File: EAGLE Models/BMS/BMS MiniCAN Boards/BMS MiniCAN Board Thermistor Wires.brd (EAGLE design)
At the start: 132.1 x 59.4 mm, 44 parts, among them IC1 AT90CAN128, IC2 MCP2551SO8, IC3 NUP2105L, IC5 FT232RL, Q1 56P2859, X10 8_PIN_CONN, X3 8_PIN_CONN, X4 8_PIN_CONN, X5 8_PIN_CONN, X6 8_PIN_CONN, X7 8_PIN_CONN, X8 8_PIN_CONN, X9 8_PIN_CONN

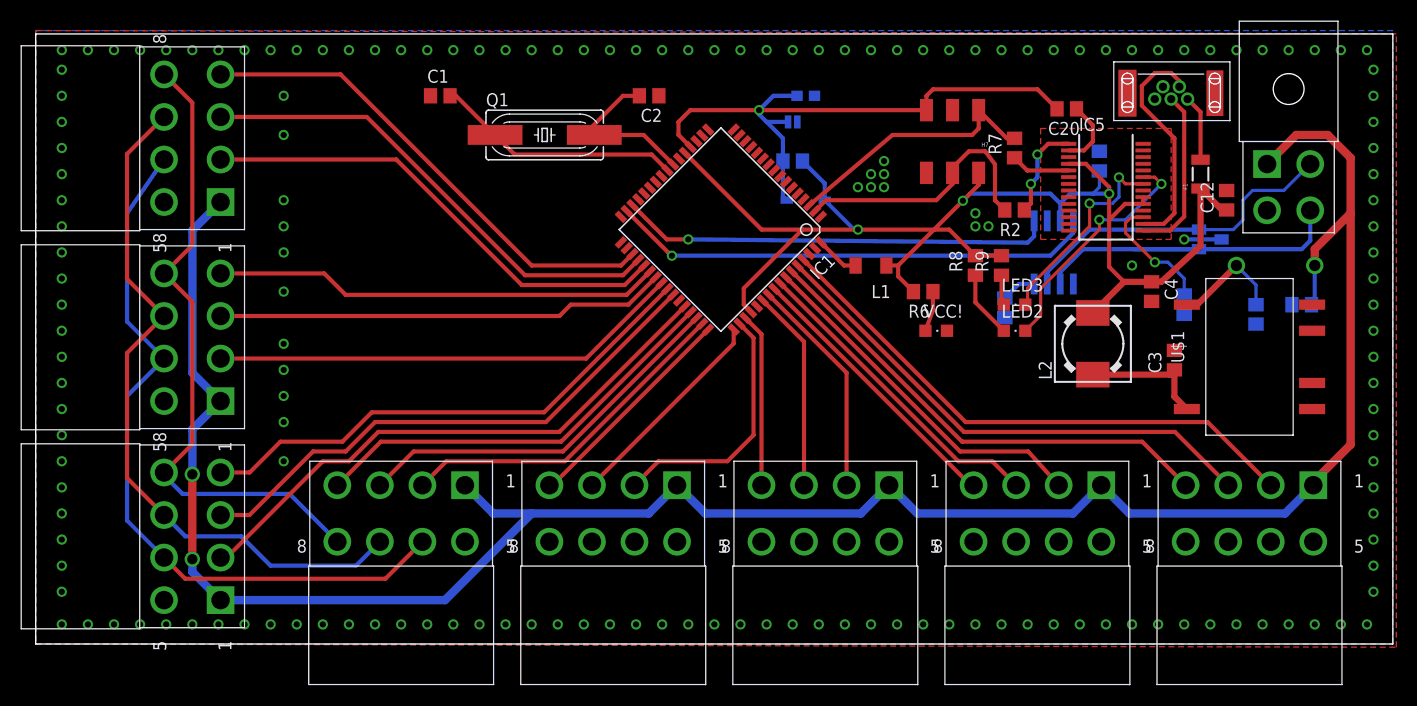
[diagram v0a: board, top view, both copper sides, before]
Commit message: Made minor changes. Added new board for different thermistor mounting strategy
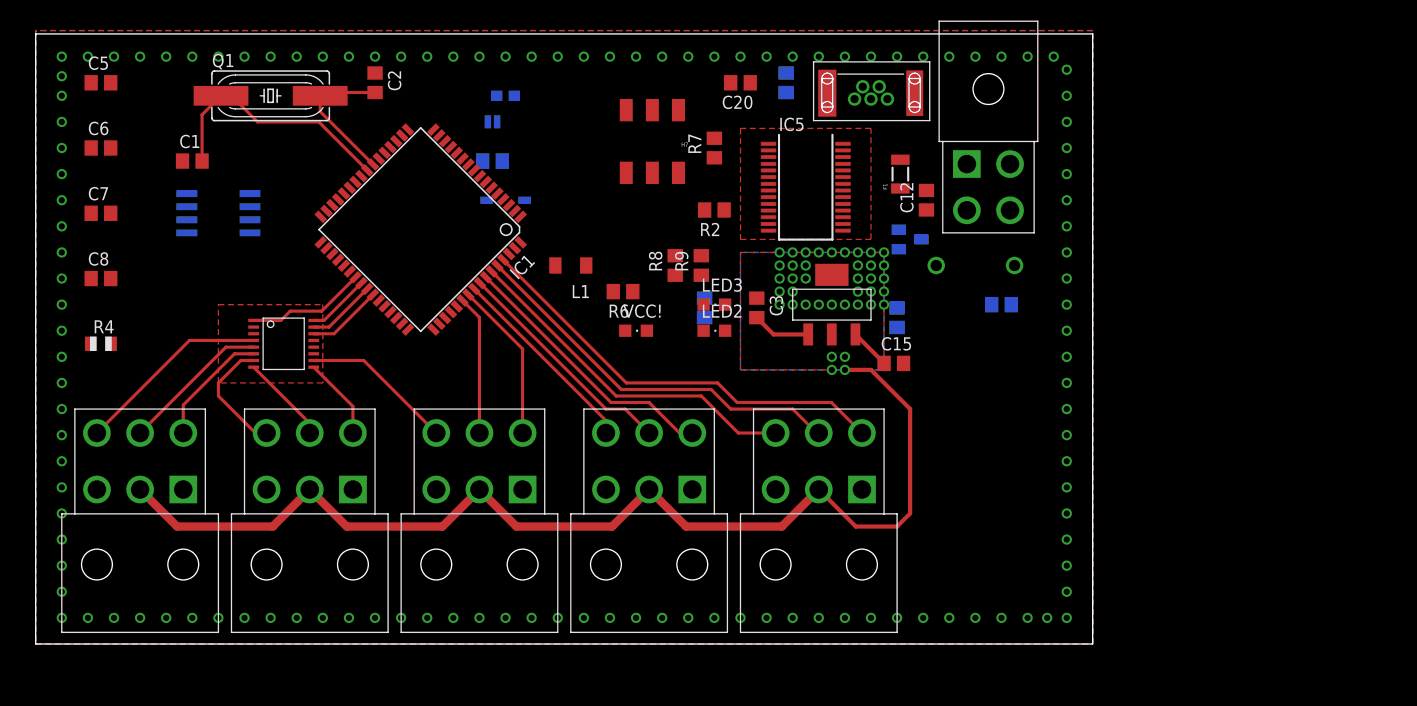
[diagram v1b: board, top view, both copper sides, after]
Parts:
- removed C4: 22uF, resistor:C0805
- removed L2: 22uH, inductors:DR73
- removed X10, X7, X8, X9: 8_PIN_CONN, BMS Lbr:8_PIN_MOLEX
- added C5, C6: .1uF, rcl:C0805
- added C7, C8: 1uF, rcl:C0805
- added R4: 51, adafruit:R0805
- added U$2: ADC084S101, BMS Lbr:TSSOP-16
- added X2: 6_PIN_CONNMOLEX_HORI, BMS Lbr:6_PIN_MOLEX
- C3: value 22uF -> 10uF
- U$1: value V7805-1000 -> LM117MPX-5.0; device formula electric:V78XX-1000 -> BMS Lbr:SOT223-4
- X3, X4, X5, X6: value 8_PIN_CONN -> 6_PIN_CONNMOLEX_HORI; device BMS Lbr:8_PIN_MOLEX -> BMS Lbr:6_PIN_MOLEX
- moved IC2 81.4 mm to (17.8, 40.6), turned to 270 degrees
- moved X3 54.4 mm to (59.7, 16.5), turned to 0 degrees
- moved C3 41.0 mm to (70.2, 31.4), turned to 270 degrees
- moved U$1 41.0 mm to (77.5, 31.8), turned to 0 degrees
- moved C15 35.6 mm to (83.5, 26.0), flipped to the top, turned to 0 degrees
- moved C20 31.9 mm to (68.6, 53.3)
- moved C19 31.4 mm to (73.0, 53.3)
- moved X4 30.4 mm to (43.2, 16.5), turned to 0 degrees
- moved C12 29.2 mm to (86.7, 41.9)
- moved C16 29.2 mm to (45.7, 52.1)
- moved D1 29.2 mm to (45.7, 41.9)
- moved D2 29.2 mm to (91.4, 35.6)
- moved R9 29.2 mm to (64.8, 35.6)
- moved X1 29.2 mm to (92.7, 43.2)
- moved H7 29.2 mm to (60.0, 47.6)
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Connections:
- removed net 12V_PROTECTED: C15.1, D2.C, U$1.1
- removed net CS10: IC1.46, X6.P$3
- removed net CS11: IC1.47, X6.P$2
- removed net CS12: IC1.48, X7.P$4
- removed net CS13: IC1.49, X7.P$3
- removed net CS14: IC1.50, X7.P$2
- removed net CS15: IC1.51, X8.P$4
- removed net CS16: IC1.54, X8.P$3
- removed net CS17: IC1.55, X8.P$2
- removed net CS18: IC1.56, X9.P$4
- removed net CS19: IC1.57, X9.P$3
- removed net CS20: IC1.58, X9.P$2
- removed net CS21: IC1.59, X10.P$4
- removed net CS22: IC1.60, X10.P$3
- removed net CS23: IC1.61, X10.P$2
- removed net CS4: IC1.39, X4.P$3
- removed net CS5: IC1.40, X4.P$2
- removed net CS6: IC1.41, X5.P$4
- removed net CS7: IC1.42, X5.P$3
- removed net CS8: IC1.44, X5.P$2
- removed net CS9: IC1.45, X6.P$4
- removed net N$13: C3.1, L2.1, U$1.5
- removed net SDI: X10.P$6, X3.P$6, X4.P$6, X5.P$6, X6.P$6, X7.P$6, X8.P$6, X9.P$6
- removed net SDO: X10.P$7, X3.P$7, X4.P$7, X5.P$7, X6.P$7, X7.P$7, X8.P$7, X9.P$7
- new net AIN0: IC1.61, X2.P$4
- new net AIN1: IC1.60, X2.P$5
- new net AIN10: U$2.P$8, X5.P$5
- new net AIN11: U$2.P$7, X5.P$6
- new net AIN12: U$2.P$6, X6.P$4
- new net AIN13: U$2.P$5, X6.P$5
- new net AIN14: U$2.P$4, X6.P$6
- new net AIN2: IC1.59, X2.P$6
- new net AIN3: IC1.58, X3.P$4
- new net AIN4: IC1.57, X3.P$5
- new net AIN5: IC1.56, X3.P$6
- new net AIN6: IC1.55, X4.P$4
- new net AIN7: IC1.54, X4.P$5
- new net AIN8: U$2.P$10, X4.P$6
- new net AIN9: U$2.P$9, X5.P$4
- new net CS: IC1.39, U$2.P$1
- new net DIN: IC1.42, U$2.P$14
- new net DOUT: IC1.41, U$2.P$15
- new net N$1: C15.1, D2.C, U$1.P$3
- new net NC: X2.P$3
- new net NC1: X3.P$3
- new net NC2: X4.P$3
- new net NC3: X5.P$3
- new net NC4: X6.P$3
- new net PA0: IC1.51
- new net PA1: IC1.50
- new net PA2: IC1.49
- new net PA3: IC1.48
- new net PA4: IC1.47
- new net PA5: IC1.46
- new net PA6: IC1.45
- new net PA7: IC1.44
- new net VD: C6.1, C8.1, R4.2, U$2.P$13
- net 12V: no longer X10.P$1, X3.P$1, X4.P$1, X5.P$1, X6.P$1, X7.P$1, X8.P$1, X9.P$1
- net CS0: no longer X3.P$4
- net CS1: no longer X3.P$3
- net CS2: no longer X3.P$2
- net CS3: no longer X4.P$4
- net GND: now also C5.2, C6.2, C7.2, C8.2, U$1.P$1, U$2.P$11, U$2.P$12, U$2.P$3, X2.P$1, X3.P$1, X4.P$1, X5.P$1, X6.P$1; no longer C4.2, U$1.7, U$1.9, X10.P$5, X3.P$5, X4.P$5, X5.P$5, X6.P$5, X7.P$5, X8.P$5, X9.P$5
- net SCLK: now also IC1.40, U$2.P$16; no longer X10.P$8, X3.P$8, X4.P$8, X5.P$8, X6.P$8, X7.P$8, X8.P$8, X9.P$8
- net VCC: now also C3.1, C5.1, C7.1, R4.1, U$1.P$2, U$1.P$4, U$2.P$2, X2.P$2, X3.P$2, X4.P$2, X5.P$2, X6.P$2; no longer C4.1, L2.2
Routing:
- net 12V: track 222.8 -> 0.00 mm, vias 2 -> 0
- net SDI: track 71.8 -> 0.00 mm
- net SDO: track 68.7 -> 0.00 mm
- net RESET: track 58.9 -> 0.00 mm, vias 1 -> 0
- net SCLK: track 63.1 -> 6.15 mm
- net CS8: track 55.3 -> 0.00 mm
- net CS23: track 54.6 -> 0.00 mm
- net CS7: track 52.9 -> 0.00 mm
- net CS6: track 50.9 -> 0.00 mm
- net CS22: track 50.7 -> 0.00 mm
- net CS0: track 48.3 -> 0.00 mm
- net CS1: track 47.7 -> 0.00 mm
- net RXCAN: track 47.3 -> 0.00 mm, vias 1 -> 0
- net CS2: track 47.1 -> 0.00 mm
- net CS21: track 46.9 -> 0.00 mm
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- added copper zone on layer 1, net VCC
- added copper zone on layer 16, net VCC
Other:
- board size 132.1 x 59.4 mm -> 102.8 x 59.4 mm

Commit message: added adc to lib
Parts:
- added U$3, U$4: MCP3008T-I/SL, BMS Lbr:16_SOIC
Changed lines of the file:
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@@
 <element name="U$1" library="BMS Lbr" package="SOT223-4" value="LM117MPX-5.0" x="77.47" y="31.75"/>
 <element name="C3" library="resistor" package="C0805" value="10uF" x="70.1675" y="31.4325" rot="R270"/>
+<element name="U$3" library="BMS Lbr" package="16_SOIC" value="MCP3008T-I/SL" x="-12.1412" y="0"/>
+<element name="U$4" library="BMS Lbr" package="16_SOIC" value="MCP3008T-I/SL" x="-11.43" y="-8.89"/>
 </elements>
 <signals>

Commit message: Fixed Multiplexer symbol
Multiplexer symbol was off the center, recentered it. Added a
multiplexer to the thermistor wires schematic. Will add more
multiplexers.
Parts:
- U$4: value MCP3008T-I/SL -> CD74HC4067; device BMS Lbr:16_SOIC -> BMS Lbr:24-SOIC
- moved U$4 6.48 mm to (-5.08, -7.62)
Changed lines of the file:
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@@
 <element name="C3" library="resistor" package="C0805" value="10uF" x="70.1675" y="31.4325" rot="R270"/>
 <element name="U$3" library="BMS Lbr" package="16_SOIC" value="MCP3008T-I/SL" x="-12.1412" y="0"/>
-<element name="U$4" library="BMS Lbr" package="16_SOIC" value="MCP3008T-I/SL" x="-11.43" y="-8.89"/>
+<element name="U$4" library="BMS Lbr" package="24-SOIC" value="CD74HC4067" x="-5.08" y="-7.62"/>
 </elements>
 <signals>

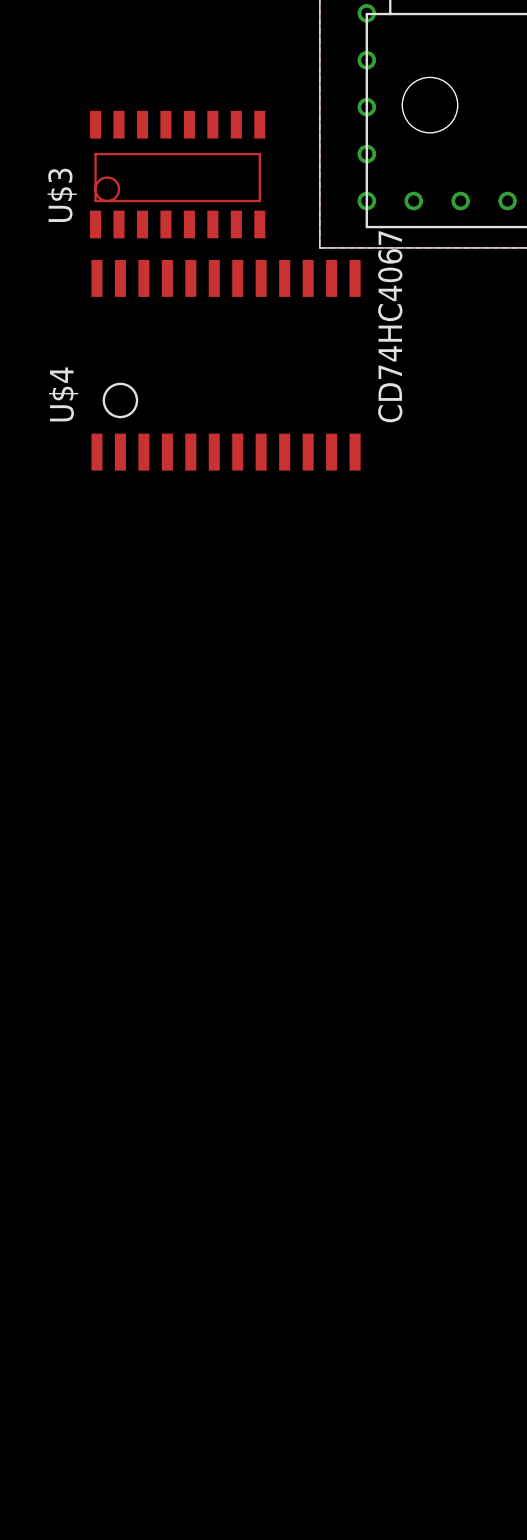
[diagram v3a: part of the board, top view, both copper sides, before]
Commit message: Added All the Muxes
Added the muxes and their respective inputs/outputs.
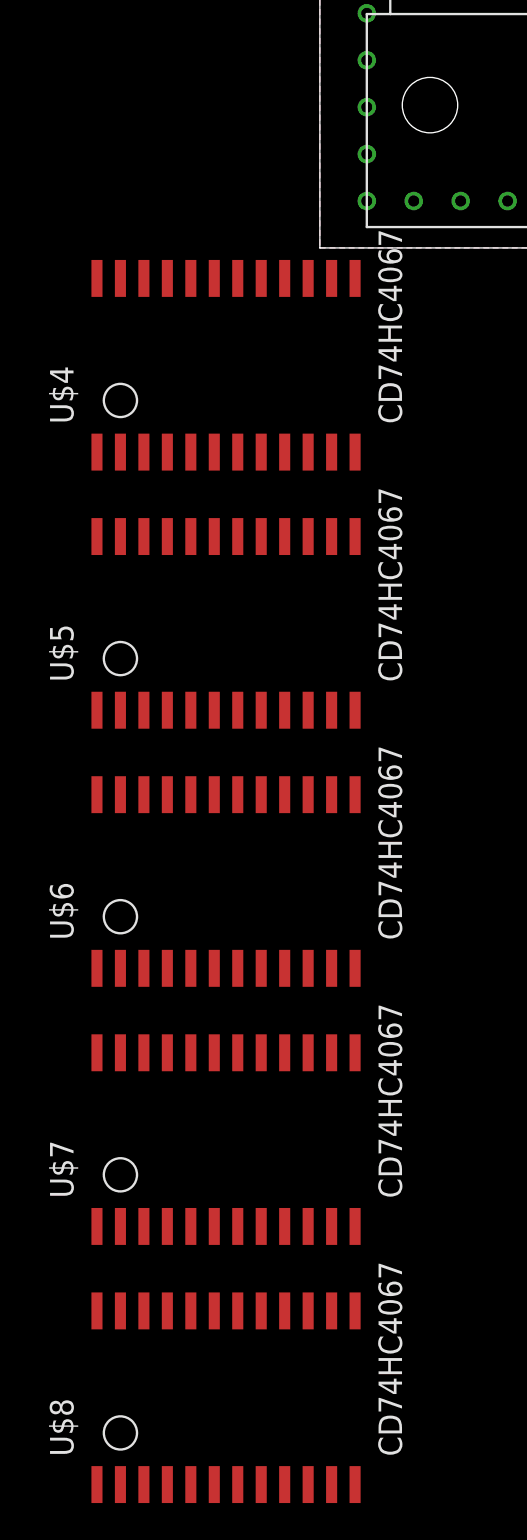
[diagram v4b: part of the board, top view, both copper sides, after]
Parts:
- removed U$3: MCP3008T-I/SL, BMS Lbr:16_SOIC
- added U$5, U$6, U$7, U$8: CD74HC4067, BMS Lbr:24-SOIC
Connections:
- new net AIN15: U$4.P$16
- new net AIN16: U$5.P$9
- new net AIN17: U$5.P$8
- new net AIN18: U$5.P$7
- new net AIN19: U$5.P$6
- new net AIN20: U$5.P$5
- new net AIN21: U$5.P$4
- new net AIN22: U$5.P$3
- new net AIN23: U$5.P$2
- new net AIN24: U$5.P$23
- new net AIN25: U$5.P$22
- new net AIN26: U$5.P$21
- new net AIN27: U$5.P$20
- new net AIN28: U$5.P$19
- new net AIN29: U$5.P$18
- new net AIN30: U$5.P$17
- new net AIN31: U$5.P$16
- new net AIN32: U$6.P$9
- new net AIN33: U$6.P$8
- new net AIN34: U$6.P$7
- new net AIN35: U$6.P$6
- new net AIN36: U$6.P$5
- new net AIN37: U$6.P$4
- new net AIN38: U$6.P$3
- new net AIN39: U$6.P$2
- new net AIN40: U$6.P$23
- new net AIN41: U$6.P$22
- new net AIN42: U$6.P$21
- new net AIN43: U$6.P$20
- new net AIN44: U$6.P$19
- new net AIN45: U$6.P$18
- new net AIN46: U$6.P$17
- new net AIN47: U$6.P$16
- new net AIN48: U$7.P$9
- new net AIN49: U$7.P$8
- new net AIN50: U$7.P$7
- new net AIN51: U$7.P$6
- new net AIN52: U$7.P$5
- new net AIN53: U$7.P$4
- new net AIN54: U$7.P$3
- new net AIN55: U$7.P$2
- new net AIN56: U$7.P$23
- new net AIN57: U$7.P$22
- new net AIN58: U$7.P$21
- new net AIN59: U$7.P$20
- new net AIN60: U$7.P$19
- new net AIN61: U$7.P$18
- new net AIN62: U$7.P$17
- new net AIN63: U$7.P$16
- new net AIN64: U$8.P$9
- new net AIN65: U$8.P$8
- new net AIN66: U$8.P$7
- new net AIN67: U$8.P$6
- new net AIN68: U$8.P$5
- new net AIN69: U$8.P$4
- new net AIN70: U$8.P$3
- new net AIN71: U$8.P$2
- new net OUT0: U$4.P$1
- new net OUT1: U$5.P$1
- new net OUT2: U$6.P$1
- new net OUT3: U$7.P$1
- new net OUT4: U$8.P$1
- new net S0: U$4.P$10, U$5.P$10, U$6.P$10, U$7.P$10, U$8.P$10
- new net S1: U$4.P$11, U$5.P$11, U$6.P$11, U$7.P$11, U$8.P$11
- new net S2: U$4.P$14, U$5.P$14, U$6.P$14, U$7.P$14, U$8.P$14
- new net S3: U$4.P$13, U$5.P$13, U$6.P$13, U$7.P$13, U$8.P$13
- net AIN0: now also U$4.P$9
- net AIN1: now also U$4.P$8
- net AIN10: now also U$4.P$21
- net AIN11: now also U$4.P$20
- net AIN12: now also U$4.P$19
- net AIN13: now also U$4.P$18
- net AIN14: now also U$4.P$17
- net AIN2: now also U$4.P$7
- net AIN3: now also U$4.P$6
- net AIN4: now also U$4.P$5
- net AIN5: now also U$4.P$4
- net AIN6: now also U$4.P$3
- net AIN7: now also U$4.P$2
- net AIN8: now also U$4.P$23
- net AIN9: now also U$4.P$22
- net GND: now also U$4.P$12, U$4.P$15, U$5.P$12, U$5.P$15, U$6.P$12, U$6.P$15, U$7.P$12, U$7.P$15, U$8.P$12, U$8.P$15, U$8.P$16, U$8.P$17, U$8.P$18, U$8.P$19, U$8.P$20, U$8.P$21, U$8.P$22, U$8.P$23
- net VCC: now also U$4.P$24, U$5.P$24, U$6.P$24, U$7.P$24, U$8.P$24

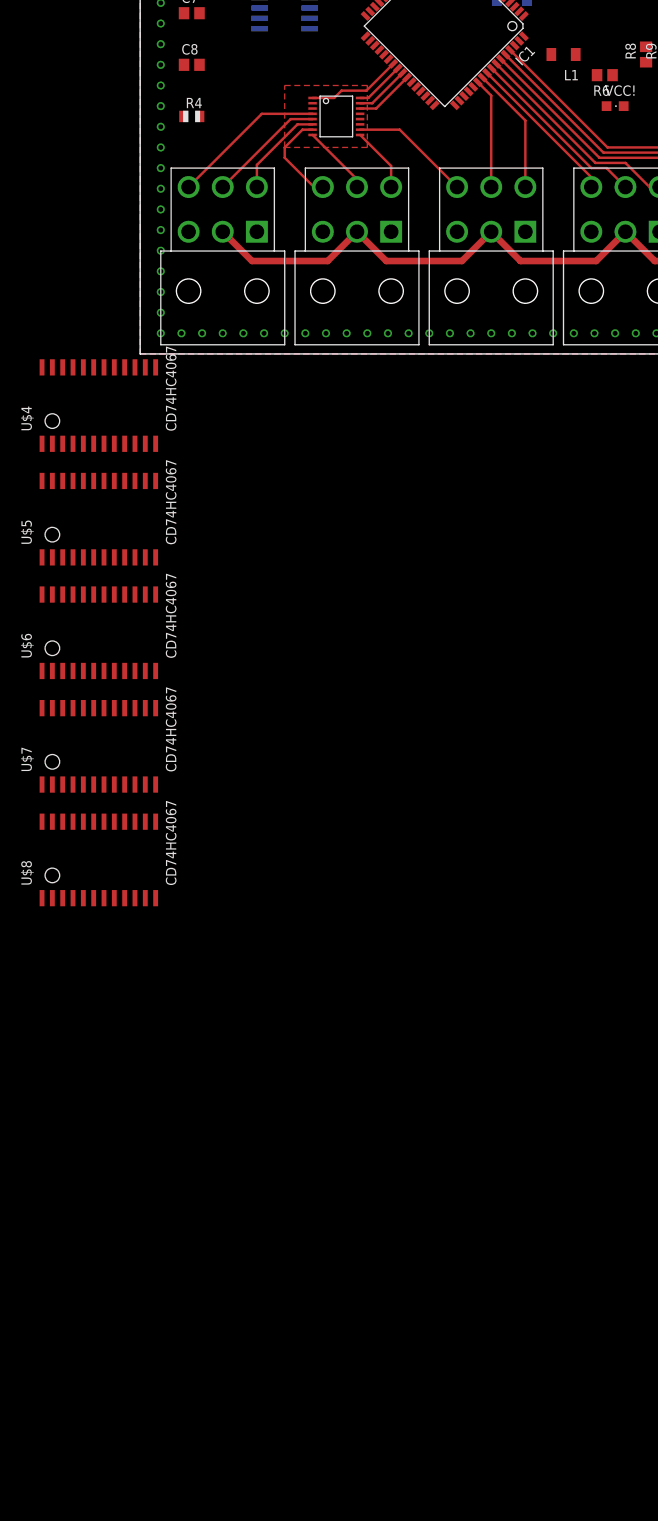
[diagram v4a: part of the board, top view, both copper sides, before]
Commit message: Added Resistors and Changed MCU I/O
Added 0603 package 10k resistors and connected muxes to the MCU
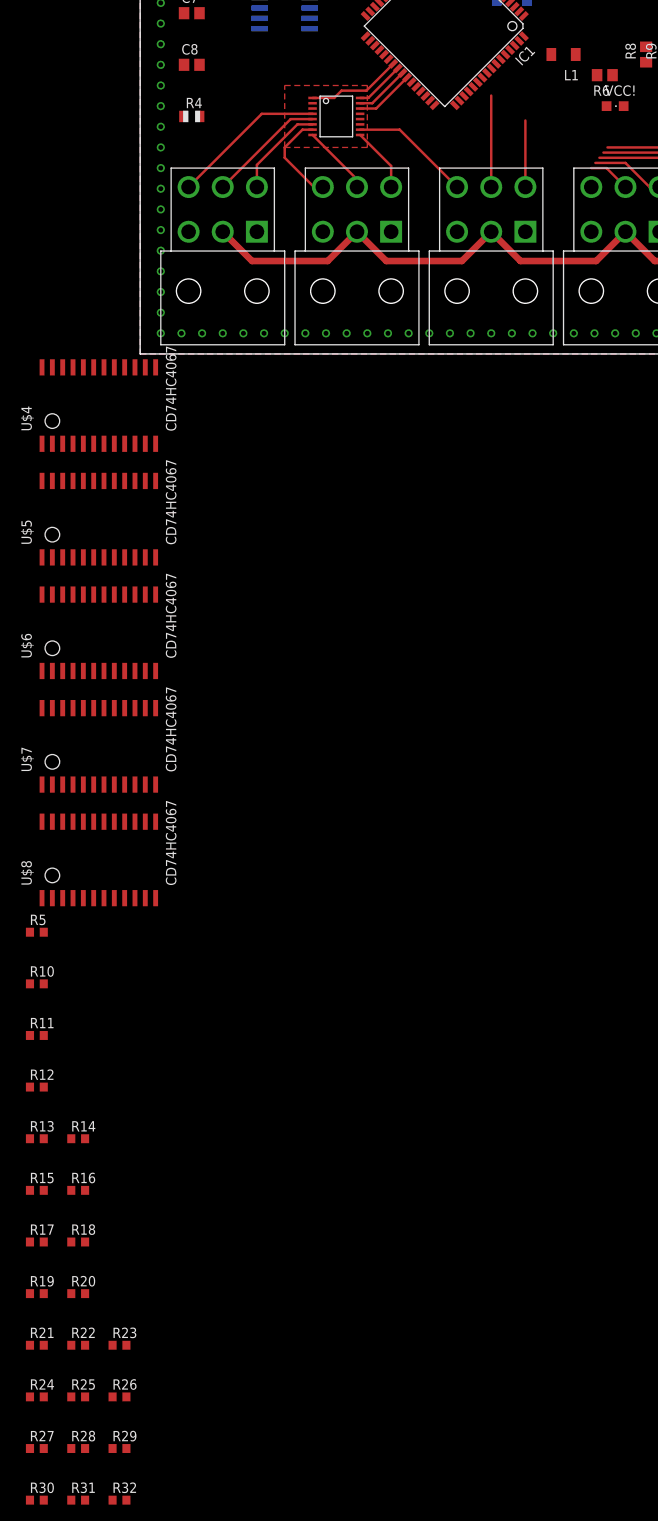
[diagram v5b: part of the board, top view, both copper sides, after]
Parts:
- added R10, R11, R12, R13, R14, R15, R16, R17, R18, R19, R20, R21, R22, R23, R24, R25, R26, R27, R28, R29, R30, R31, R32, R5: 10K, adafruit:R0603
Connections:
- removed net CS0: IC1.35
- removed net CS1: IC1.36
- removed net CS2: IC1.37
- removed net CS3: IC1.38
- removed net SCK: H7.3
- net AIN0: no longer IC1.61
- net AIN1: no longer IC1.60
- net AIN2: no longer IC1.59
- net AIN3: no longer IC1.58
- net AIN4: no longer IC1.57
- net AIN5: no longer IC1.56
- net AIN6: no longer IC1.55
- net AIN7: no longer IC1.54
- net AVR_SCK: now also H7.3
- net GND: now also IC1.54, IC1.55, IC1.56, R10.2, R11.2, R12.2, R13.2, R14.2, R15.2, R16.2, R17.2, R18.2, R19.2, R20.2, R21.2, R22.2, R23.2, R24.2, R25.2, R26.2, R27.2, R28.2, R29.2, R30.2, R31.2, R32.2, R5.2
- net OUT0: now also IC1.61
- net OUT1: now also IC1.60
- net OUT2: now also IC1.59
- net OUT3: now also IC1.58
- net OUT4: now also IC1.57
- net S0: now also IC1.35
- net S1: now also IC1.36
- net S2: now also IC1.37
- net S3: now also IC1.38
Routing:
- net AIN5: track 19.3 -> 1.20 mm
- net AIN4: track 22.5 -> 5.16 mm
- net AIN3: track 26.4 -> 9.13 mm
- net AIN2: track 34.1 -> 17.0 mm
- net AIN1: track 38.0 -> 21.0 mm
- net AIN0: track 41.9 -> 24.9 mm
- net AIN6: track 15.6 -> 8.18 mm
- net AIN7: track 13.6 -> 11.2 mm
